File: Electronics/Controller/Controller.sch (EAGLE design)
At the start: 16 parts, among them Q1 BS250, U1 GY-521MPU6050, X1 Battery

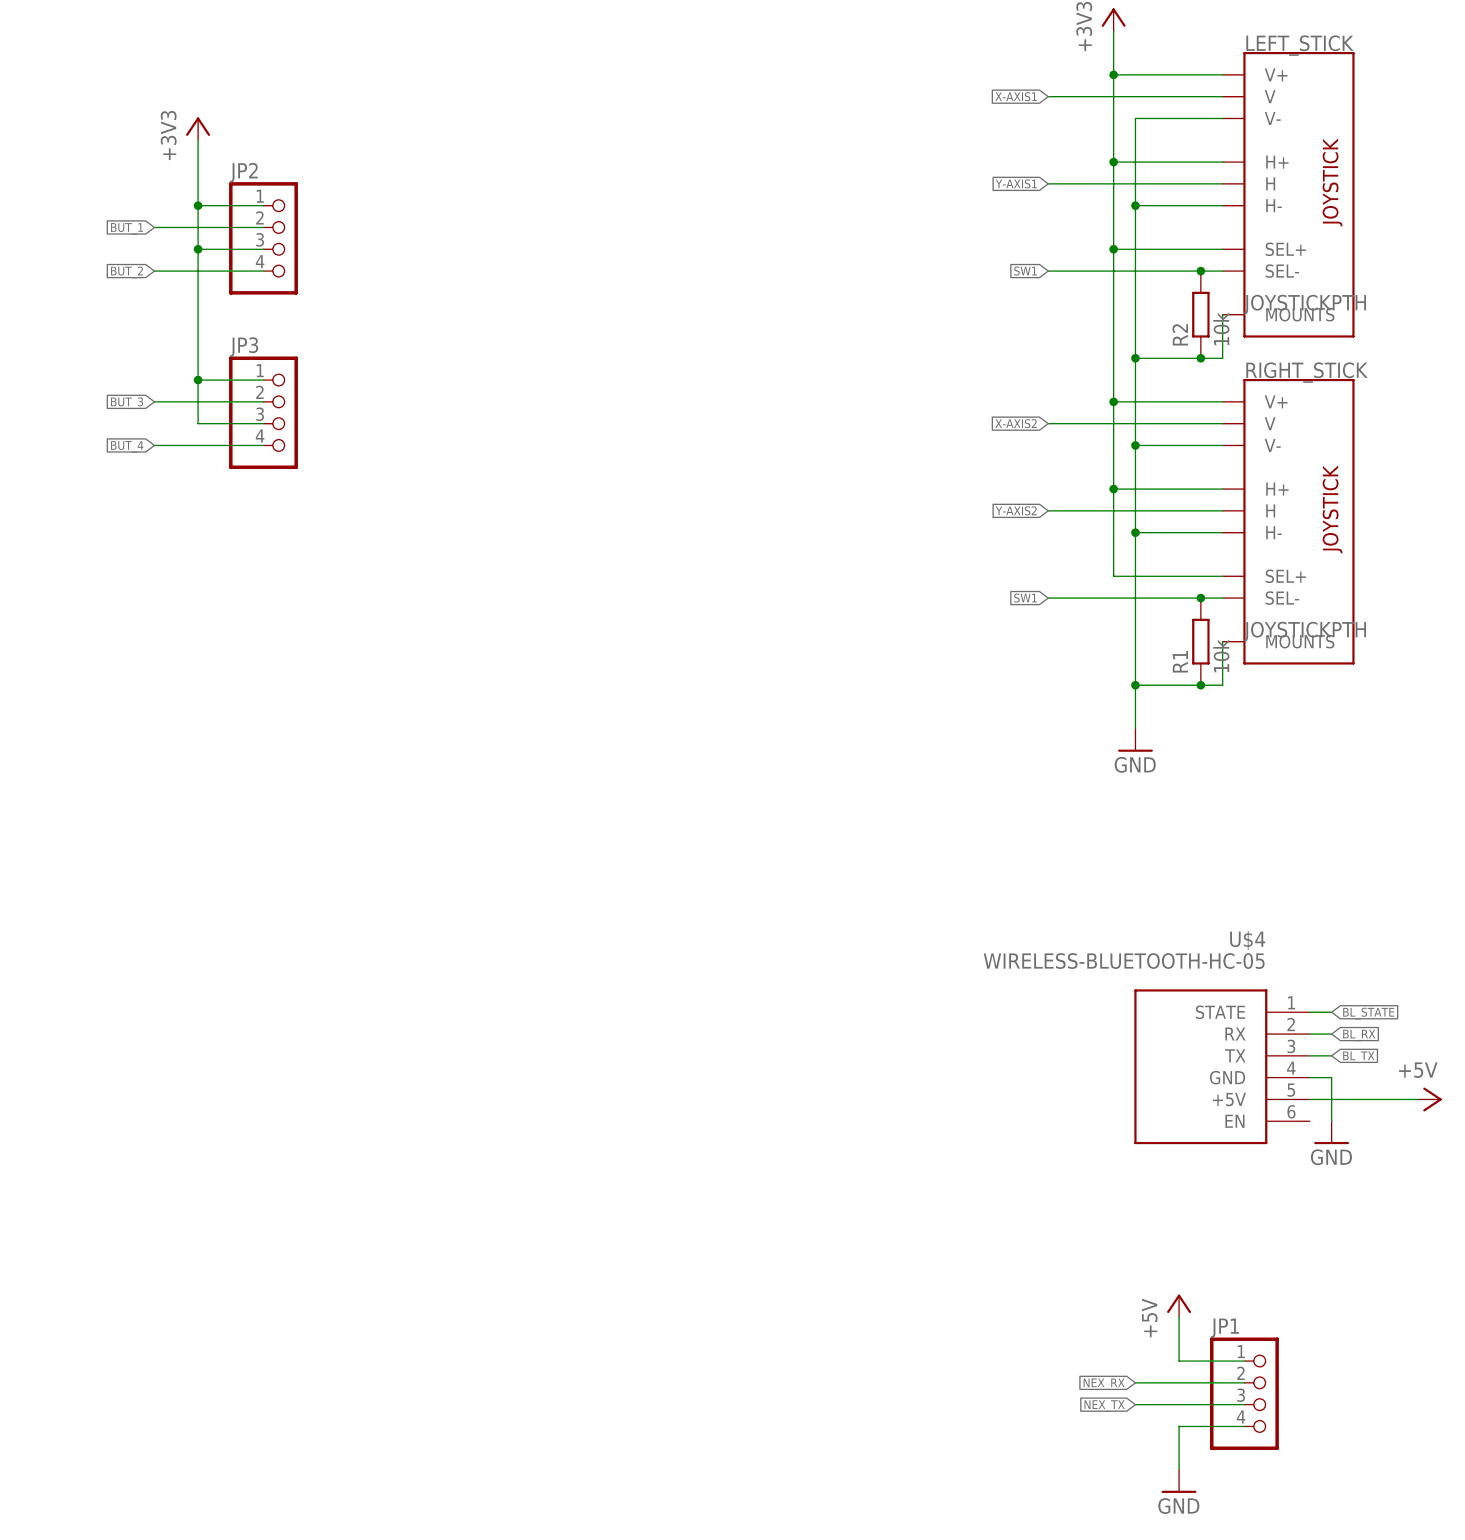
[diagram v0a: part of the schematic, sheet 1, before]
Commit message: Automatic source change
Added automatic source change and fixing librabry's for better overview
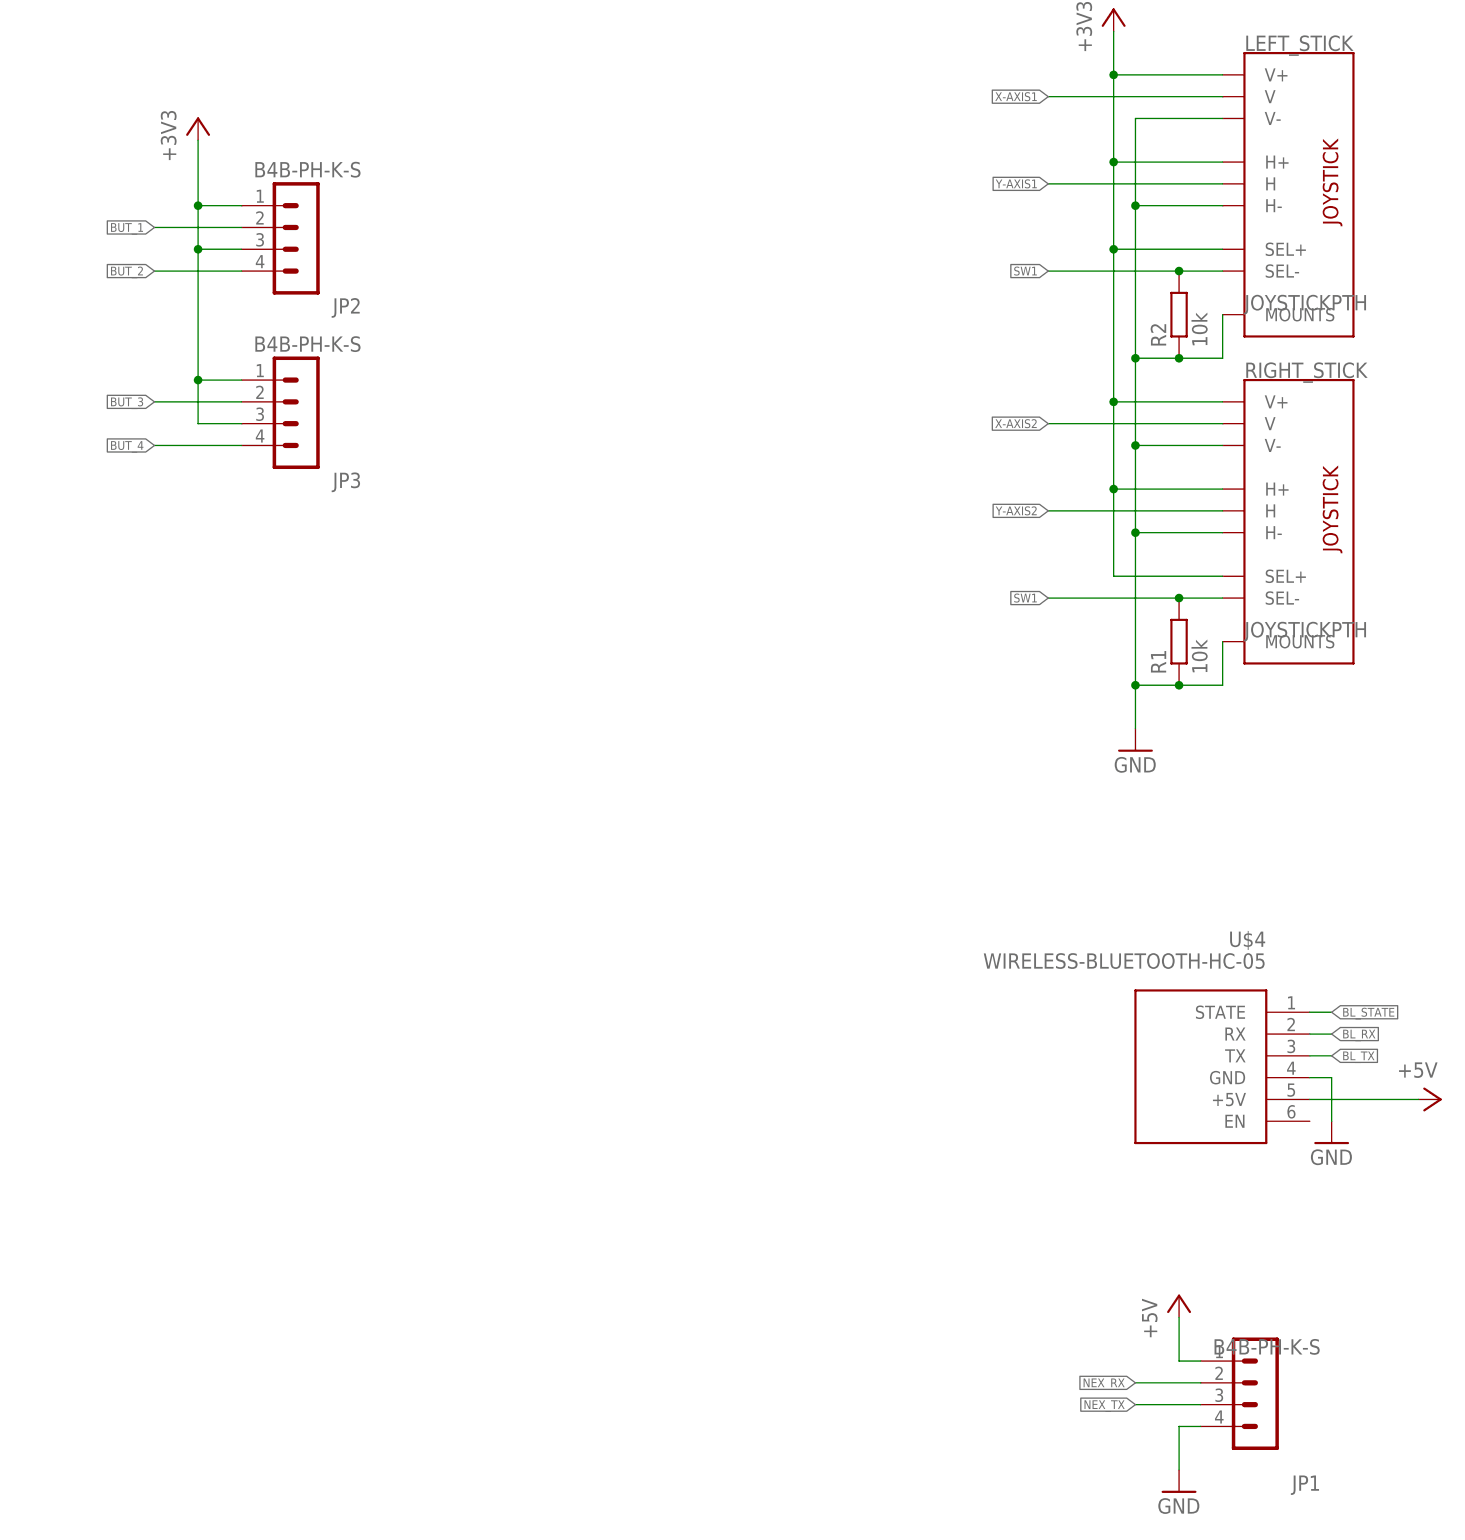
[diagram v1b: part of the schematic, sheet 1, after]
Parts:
- added X2: Switch, con-JST PH:B2B-PH-K-S
- JP1, JP2, JP3: value (none) -> B4B-PH-K-S; device pinhead:PINHD-1X4 -> con-JST PH:B4B-PH-K-S
- Q1: value BS250 -> IRFD9014; device transistor-small-signal:BS250 -> transistor-small-signal:IRFD9120
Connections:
- new net N$6: U$8.IN+, X2.2
- net +5V: now also U$8.OUT+; no longer U$8.IN+
- net GND: now also U$8.OUT-; no longer U$8.IN-
- net N$1: now also U$8.IN-; no longer U$8.OUT-
- net N$4: now also X2.1; no longer U$8.OUT+
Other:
- moved on the sheet: D1, R1, R2, R3, U$8

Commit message: Buzzer, Teensy 4.0 Robot
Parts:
- added R4: 2K2, rcl:R-EU_0207/10
- added SG1: F/EE17P, buzzer:F/EE17P
- added T1: (no value), transistor:-NPN-TO92-EBC
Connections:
- new net BUZZER: R4.1, U$1.4/T/PWM
- new net N$7: R4.2, T1.B
- new net N$8: SG1.2, T1.C
- net +5V: now also SG1.1
- net GND: now also T1.E
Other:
- note added: "Buzzer"
- moved on the sheet: U$4
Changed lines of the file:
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@@
 <?xml version="1.0" encoding="utf-8"?>
 <!DOCTYPE eagle SYSTEM "eagle.dtd">
-<eagle version="9.6.2">
+<eagle version="9.6.1">
 <drawing>
 <settings>
@@
 <layer number="97" name="Info" color="7" fill="1" visible="yes" active="yes"/>
 <layer number="98" name="Guide" color="6" fill="1" visible="yes" active="yes"/>
-<layer number="99" name="SpiceOrder" color="7" fill="1" visible="no" active="yes"/>
+<layer number="99" name="SpiceOrder" color="7" fill="1" visible="yes" active="yes"/>
 <layer number="100" name="Muster" color="7" fill="1" visible="no" active="no"/>
 <layer number="101" name="Patch_Top" color="12" fill="4" visible="no" active="yes"/>
@@
 <layer number="112" name="tSilk" color="7" fill="1" visible="no" active="yes"/>
 <layer number="113" name="IDFDebug" color="4" fill="1" visible="no" active="yes"/>
-<layer number="114" name="Badge_Outline" color="7" fill="1" visible="yes" active="yes"/>
-<layer number="115" name="ReferenceISLANDS" color="7" fill="1" visible="yes" active="yes"/>
+<layer number="114" name="Badge_Outline" color="7" fill="1" visible="no" active="yes"/>
+<layer number="115" name="ReferenceISLANDS" color="7" fill="1" visible="no" active="yes"/>
 <layer number="116" name="Patch_BOT" color="9" fill="4" visible="no" active="yes"/>
+<layer number="117" name="BOX" color="8" fill="0" visible="yes" active="yes"/>
 <layer number="118" name="Rect_Pads" color="7" fill="1" visible="no" active="yes"/>
 <layer number="121" name="_tsilk" color="7" fill="1" visible="no" active="yes"/>
@@
 <layer number="230" name="230bmp" color="7" fill="1" visible="no" active="yes"/>
 <layer number="231" name="231bmp" color="7" fill="1" visible="no" active="yes"/>
-<layer number="232" name="Eagle3D_PG2" color="7" fill="1" visible="yes" active="yes"/>
-<layer number="233" name="Eagle3D_PG3" color="7" fill="1" visible="yes" active="yes"/>
+<layer number="232" name="Eagle3D_PG2" color="7" fill="1" visible="no" active="yes"/>
+<layer number="233" name="Eagle3D_PG3" color="7" fill="1" visible="no" active="yes"/>
 <layer number="248" name="Housing" color="7" fill="1" visible="no" active="yes"/>
 <layer number="249" name="Edge" color="7" fill="1" visible="no" active="yes"/>
@@
 <part name="X1" library="con-JST PH" deviceset="B2B-PH" device="-K-S" value="Battery"/>
 <part name="X2" library="con-JST PH" deviceset="B2B-PH" device="-K-S" value="Switch"/>
+<part name="SG1" library="buzzer" library_urn="urn:adsk.eagle:library:113" deviceset="F/EE17P" device="" package3d_urn="urn:adsk.eagle:package:5285/1"/>
+<part name="T1" library="transistor" library_urn="urn:adsk.eagle:library:402" deviceset="*-NPN-" device="TO92-EBC" package3d_urn="urn:adsk.eagle:package:29915/2"/>
+<part name="R4" library="rcl" library_urn="urn:adsk.eagle:library:334" deviceset="R-EU_" device="0207/10" package3d_urn="urn:adsk.eagle:package:23491/2" value="2K2"/>
+<part name="P+5" library="supply1" library_urn="urn:adsk.eagle:library:371" deviceset="+5V" device=""/>
+<part name="GND8" library="supply1" library_urn="urn:adsk.eagle:library:371" deviceset="GND" device=""/>
 </parts>
 <sheets>
 <sheet>
 <plain>
+<text x="22.86" y="63.5" size="3.81" layer="97">Buzzer</text>
+<rectangle x1="17.78" y1="17.78" x2="99.06" y2="71.12" layer="117"/>
 </plain>
 <instances>
@@
 <attribute name="VALUE" x="320.04" y="236.22" size="1.778" layer="96" rot="R90"/>
 </instance>
-<instance part="GND6" gate="1" x="347.98" y="109.22" smashed="yes">
-<attribute name="VALUE" x="345.44" y="106.68" size="1.778" layer="96"/>
-</instance>
-<instance part="P+1" gate="1" x="360.68" y="114.3" smashed="yes" rot="R270">
-<attribute name="VALUE" x="355.6" y="116.84" size="1.778" layer="96"/>
+<instance part="GND6" gate="1" x="342.9" y="111.76" smashed="yes">
+<attribute name="VALUE" x="340.36" y="109.22" size="1.778" layer="96"/>
+</instance>
+<instance part="P+1" gate="1" x="355.6" y="116.84" smashed="yes" rot="R270">
+<attribute name="VALUE" x="350.52" y="119.38" size="1.778" layer="96"/>
 </instance>
 <instance part="U$1" gate="G$1" x="66.04" y="190.5" smashed="yes">
@@
 <attribute name="VALUE" x="63.246" y="152.4" size="1.27" layer="96" font="vector" ratio="15"/>
 </instance>
-<instance part="U$4" gate="G$1" x="325.12" y="119.38" smashed="yes" rot="MR0">
-<attribute name="NAME" x="340.36" y="132.08" size="1.778" layer="95" rot="MR0"/>
-<attribute name="VALUE" x="340.36" y="129.54" size="1.778" layer="96" rot="MR0"/>
+<instance part="U$4" gate="G$1" x="320.04" y="121.92" smashed="yes" rot="MR0">
+<attribute name="NAME" x="335.28" y="134.62" size="1.778" layer="95" rot="MR0"/>
+<attribute name="VALUE" x="335.28" y="132.08" size="1.778" layer="96" rot="MR0"/>
 </instance>
 <instance part="U1" gate="G$1" x="73.66" y="111.76" smashed="yes" rot="MR0"/>
@@
 <instance part="+3V4" gate="G$1" x="215.9" y="228.6" smashed="yes">
 <attribute name="VALUE" x="213.36" y="223.52" size="1.778" layer="96" rot="R90"/>
+</instance>
+<instance part="SG1" gate="G$1" x="60.96" y="50.8" smashed="yes">
+<attribute name="NAME" x="58.42" y="57.15" size="1.778" layer="95"/>
+<attribute name="VALUE" x="67.31" y="50.8" size="1.778" layer="96"/>
+</instance>
+<instance part="T1" gate="G$1" x="66.04" y="38.1" smashed="yes">
+<attribute name="NAME" x="64.262" y="41.91" size="1.778" layer="95"/>
+<attribute name="VALUE" x="55.88" y="43.18" size="1.778" layer="96"/>
+</instance>
+<instance part="R4" gate="G$1" x="55.88" y="38.1" smashed="yes">
+<attribute name="NAME" x="52.07" y="39.5986" size="1.778" layer="95"/>
+<attribute name="VALUE" x="52.07" y="34.798" size="1.778" layer="96"/>
+</instance>
+<instance part="P+5" gate="1" x="43.18" y="48.26" smashed="yes" rot="R90">
+<attribute name="VALUE" x="48.26" y="45.72" size="1.778" layer="96" rot="R180"/>
+</instance>
+<instance part="GND8" gate="1" x="68.58" y="27.94" smashed="yes">
+<attribute name="VALUE" x="66.04" y="25.4" size="1.778" layer="96"/>
 </instance>
 </instances>
@@
 <segment>
 <pinref part="GND6" gate="1" pin="GND"/>
-<wire x1="347.98" y1="111.76" x2="347.98" y2="116.84" width="0.1524" layer="91"/>
-<wire x1="347.98" y1="116.84" x2="345.44" y2="116.84" width="0.1524" layer="91"/>
+<wire x1="342.9" y1="114.3" x2="342.9" y2="119.38" width="0.1524" layer="91"/>
+<wire x1="342.9" y1="119.38" x2="340.36" y2="119.38" width="0.1524" layer="91"/>
 <pinref part="U$4" gate="G$1" pin="GND"/>
 </segment>
@@
 <wire x1="330.2" y1="71.12" x2="330.2" y2="76.2" width="0.1524" layer="91"/>
 <wire x1="330.2" y1="76.2" x2="332.74" y2="76.2" width="0.1524" layer="91"/>
+</segment>
+<segment>
+<pinref part="T1" gate="G$1" pin="E"/>
+<wire x1="68.58" y1="33.02" x2="68.58" y2="30.48" width="0.1524" layer="91"/>
+<pinref part="GND8" gate="1" pin="GND"/>
 </segment>
 </net>
@@
 <segment>
 <pinref part="P+1" gate="1" pin="+5V"/>
-<wire x1="345.44" y1="114.3" x2="358.14" y2="114.3" width="0.1524" layer="91"/>
+<wire x1="340.36" y1="116.84" x2="353.06" y2="116.84" width="0.1524" layer="91"/>
 <pinref part="U$4" gate="G$1" pin="+5V"/>
 </segment>
@@
 <wire x1="330.2" y1="83.82" x2="330.2" y2="88.9" width="0.1524" layer="91"/>
 </segment>
+<segment>
+<pinref part="SG1" gate="G$1" pin="1"/>
+<wire x1="58.42" y1="48.26" x2="45.72" y2="48.26" width="0.1524" layer="91"/>
+<pinref part="P+5" gate="1" pin="+5V"/>
+</segment>
 </net>
 <net name="BL_TX" class="0">
 <segment>
-<wire x1="345.44" y1="119.38" x2="347.98" y2="119.38" width="0.1524" layer="91"/>
-<label x="347.98" y="119.38" size="1.016" layer="95" xref="yes"/>
+<wire x1="340.36" y1="121.92" x2="342.9" y2="121.92" width="0.1524" layer="91"/>
+<label x="342.9" y="121.92" size="1.016" layer="95" xref="yes"/>
 <pinref part="U$4" gate="G$1" pin="TX"/>
 </segment>
@@
 <net name="BL_RX" class="0">
 <segment>
-<wire x1="345.44" y1="121.92" x2="347.98" y2="121.92" width="0.1524" layer="91"/>
-<label x="347.98" y="121.92" size="1.016" layer="95" xref="yes"/>
+<wire x1="340.36" y1="124.46" x2="342.9" y2="124.46" width="0.1524" layer="91"/>
+<label x="342.9" y="124.46" size="1.016" layer="95" xref="yes"/>
 <pinref part="U$4" gate="G$1" pin="RX"/>
 </segment>
@@
 <net name="BL_STATE" class="0">
 <segment>
-<wire x1="345.44" y1="124.46" x2="347.98" y2="124.46" width="0.1524" layer="91"/>
-<label x="347.98" y="124.46" size="1.016" layer="95" xref="yes"/>
+<wire x1="340.36" y1="127" x2="342.9" y2="127" width="0.1524" layer="91"/>
+<label x="342.9" y="127" size="1.016" layer="95" xref="yes"/>
 <pinref part="U$4" gate="G$1" pin="STATE"/>
 </segment>
@@
 </segment>
 </net>
+<net name="N$7" class="0">
+<segment>
+<pinref part="R4" gate="G$1" pin="2"/>
+<pinref part="T1" gate="G$1" pin="B"/>
+<wire x1="60.96" y1="38.1" x2="63.5" y2="38.1" width="0.1524" layer="91"/>
+</segment>
+</net>
+<net name="N$8" class="0">
+<segment>
+<pinref part="T1" gate="G$1" pin="C"/>
+<pinref part="SG1" gate="G$1" pin="2"/>
+<wire x1="68.58" y1="43.18" x2="68.58" y2="48.26" width="0.1524" layer="91"/>
+<wire x1="68.58" y1="48.26" x2="66.04" y2="48.26" width="0.1524" layer="91"/>
+</segment>
+</net>
+<net name="BUZZER" class="0">
+<segment>
+<pinref part="R4" gate="G$1" pin="1"/>
+<wire x1="50.8" y1="38.1" x2="48.26" y2="38.1" width="0.1524" layer="91"/>
+<label x="48.26" y="38.1" size="1.778" layer="95" rot="R180" xref="yes"/>
+</segment>
+<segment>
+<wire x1="43.18" y1="208.28" x2="35.56" y2="208.28" width="0.1524" layer="91"/>
+<label x="35.56" y="208.28" size="1.016" layer="95" rot="R180" xref="yes"/>
+<pinref part="U$1" gate="G$1" pin="4/T/PWM"/>
+</segment>
+</net>
